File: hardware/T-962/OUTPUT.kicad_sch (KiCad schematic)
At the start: 21 parts

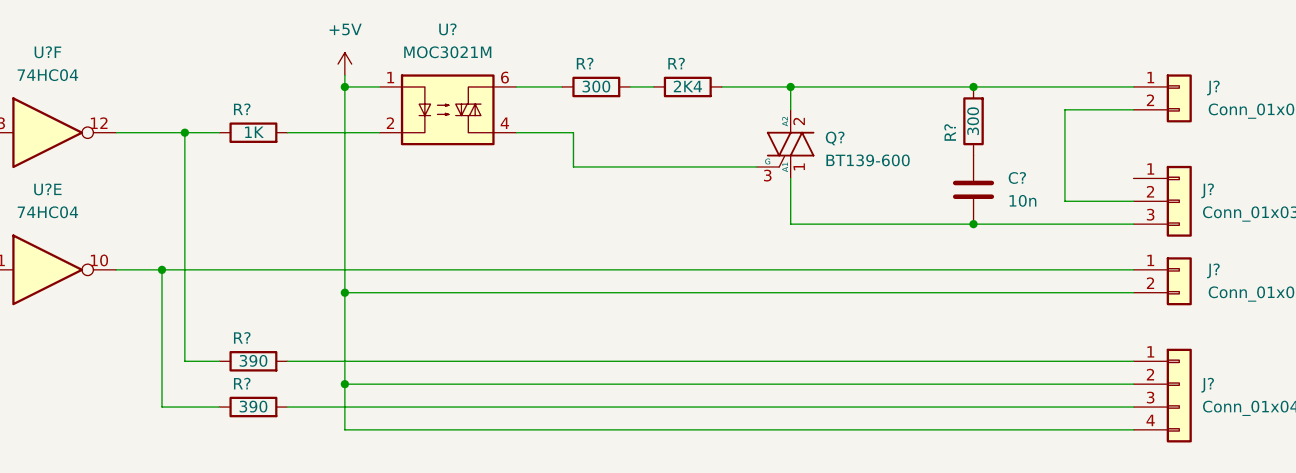
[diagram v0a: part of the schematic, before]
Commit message: add max31850 thermocouple interfaces
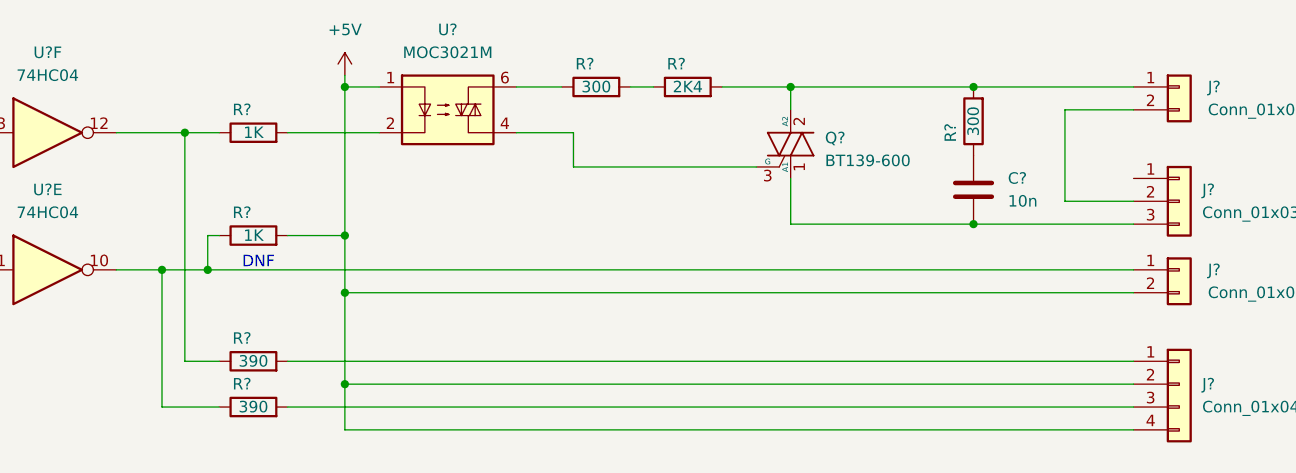
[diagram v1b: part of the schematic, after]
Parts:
- added R?: 1K, symbol Device:R
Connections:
- net +5V: now also R?.2
- net at J?.1 (Pin_1), R?.1, U?.10: now also R?.1
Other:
- note added: "DNF"
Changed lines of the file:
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@@
   (junction (at 144.78 101.6) (diameter 0) (color 0 0 0 0)
   )
+  (junction (at 129.54 99.06) (diameter 0) (color 0 0 0 0)
+  )
   (junction (at 102.87 133.35) (diameter 0) (color 0 0 0 0)
   )
@@
   )
   (junction (at 144.78 111.76) (diameter 0) (color 0 0 0 0)
+  )
+  (junction (at 144.78 95.25) (diameter 0) (color 0 0 0 0)
   )
   (no_connect (at 124.46 148.59))
@@
     (stroke (width 0) (type default) (color 0 0 0 0))
   )
+  (wire (pts (xy 129.54 95.25) (xy 129.54 99.06))
+    (stroke (width 0) (type default) (color 0 0 0 0))
+  )
+  (wire (pts (xy 130.81 95.25) (xy 129.54 95.25))
+    (stroke (width 0) (type default) (color 0 0 0 0))
+  )
+  (wire (pts (xy 129.54 99.06) (xy 232.41 99.06))
+    (stroke (width 0) (type default) (color 0 0 0 0))
+  )
   (wire (pts (xy 148.59 78.74) (xy 144.78 78.74))
     (stroke (width 0) (type default) (color 0 0 0 0))
@@
     (stroke (width 0) (type default) (color 0 0 0 0))
   )
+  (wire (pts (xy 138.43 95.25) (xy 144.78 95.25))
+    (stroke (width 0) (type default) (color 0 0 0 0))
+  )
   (wire (pts (xy 68.58 99.06) (xy 82.55 99.06))
     (stroke (width 0) (type default) (color 0 0 0 0))
@@
     (stroke (width 0) (type default) (color 0 0 0 0))
   )
-  (wire (pts (xy 144.78 78.74) (xy 144.78 101.6))
+  (wire (pts (xy 144.78 78.74) (xy 144.78 95.25))
     (stroke (width 0) (type default) (color 0 0 0 0))
   )
@@
     (stroke (width 0) (type default) (color 0 0 0 0))
   )
+  (wire (pts (xy 144.78 95.25) (xy 144.78 101.6))
+    (stroke (width 0) (type default) (color 0 0 0 0))
+  )
   (wire (pts (xy 194.31 93.98) (xy 194.31 88.9))
     (stroke (width 0) (type default) (color 0 0 0 0))
@@
     (stroke (width 0) (type default) (color 0 0 0 0))
   )
-  (wire (pts (xy 124.46 99.06) (xy 232.41 99.06))
-    (stroke (width 0) (type default) (color 0 0 0 0))
-  )
   (wire (pts (xy 138.43 109.22) (xy 232.41 109.22))
     (stroke (width 0) (type default) (color 0 0 0 0))
@@
     (stroke (width 0) (type default) (color 0 0 0 0))
   )
+  (wire (pts (xy 124.46 99.06) (xy 129.54 99.06))
+    (stroke (width 0) (type default) (color 0 0 0 0))
+  )
   (text "220VAC" (at 254 91.44 0)
     (effects (font (size 1.27 1.27)) (justify left bottom))
@@
   )
   (text "COOLING FAN" (at 254 81.28 0)
+    (effects (font (size 1.27 1.27)) (justify left bottom))
+  )
+  (text "DNF" (at 133.35 99.06 0)
     (effects (font (size 1.27 1.27)) (justify left bottom))
   )
@@
       (effects (font (size 1.27 1.27)) hide)
     )
+    (pin "1")
+    (pin "2")
+  )
+  (symbol (lib_id "Device:R") (at 134.62 95.25 90) (unit 1)
+    (in_bom yes) (on_board yes)
+    (property "Reference" "R?" (id 0) (at 133.35 92.71 90))
+    (property "Value" "1K" (id 1) (at 134.62 95.25 90))
+    (property "Footprint" "" (id 2) (at 134.62 97.028 90)
+      (effects (font (size 1.27 1.27)) hide)
+    )
+    (property "Datasheet" "~" (id 3) (at 134.62 95.25 0)
+      (effects (font (size 1.27 1.27)) hide)
+    )

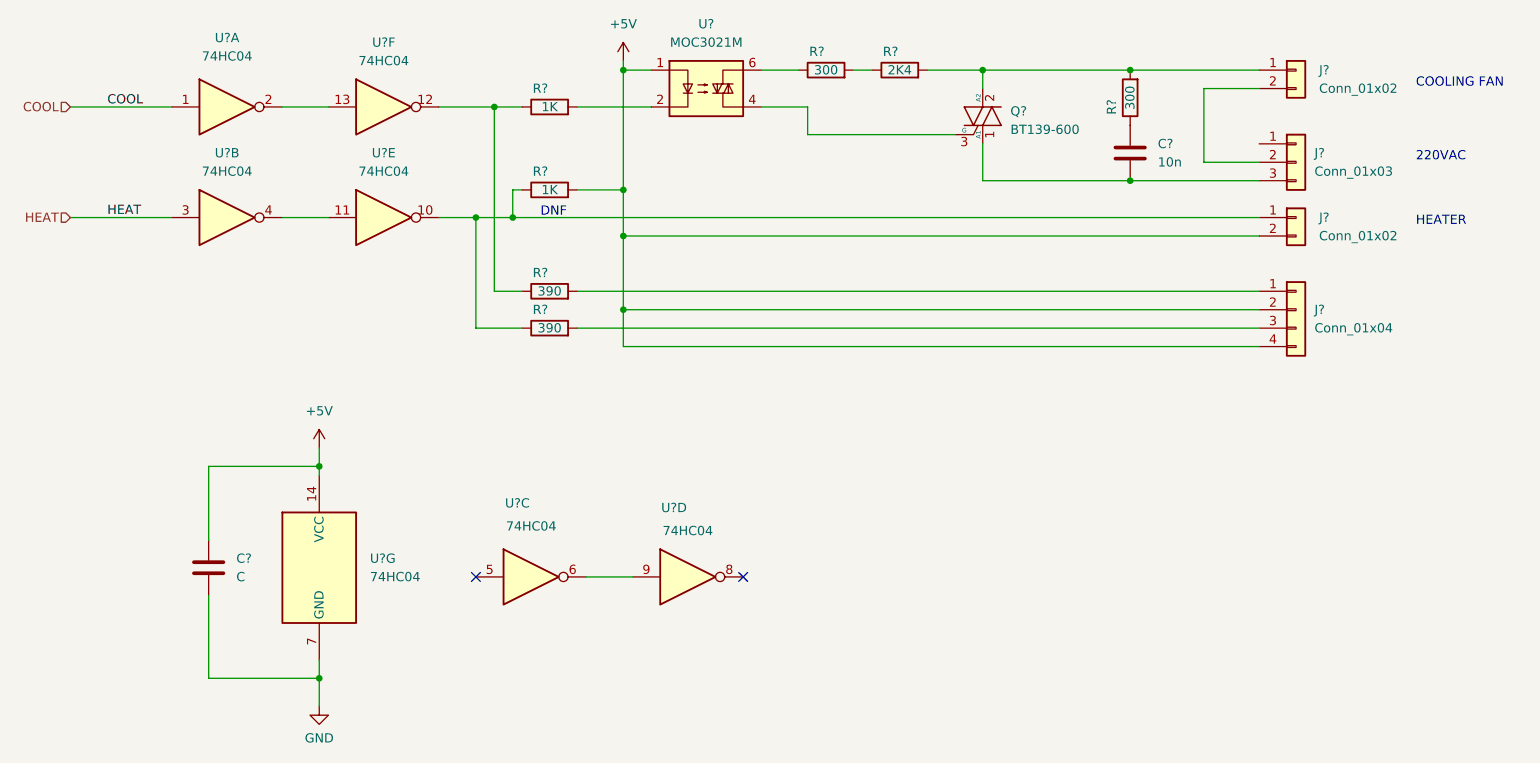
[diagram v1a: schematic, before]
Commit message: fill out designators
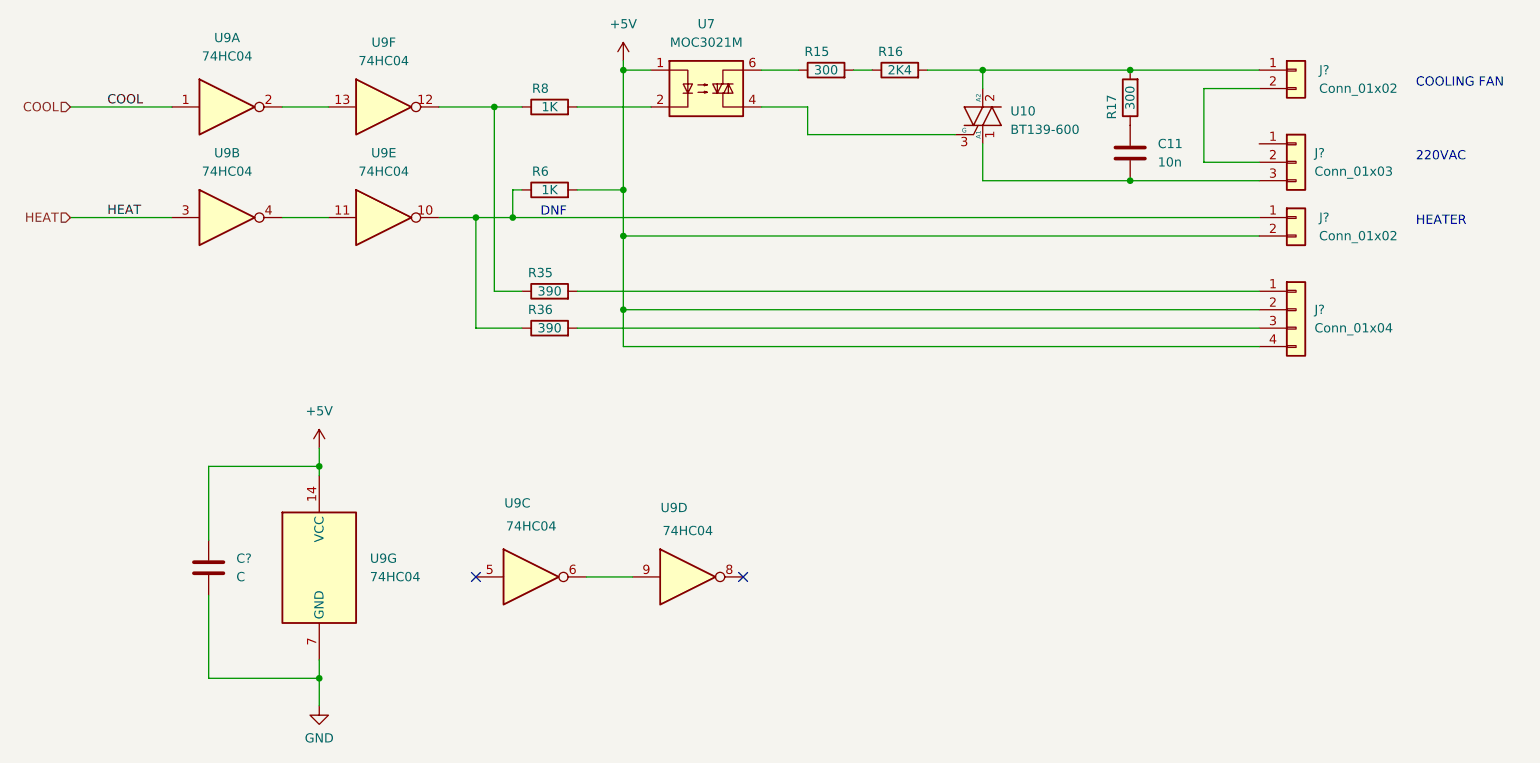
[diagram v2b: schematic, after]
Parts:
- gave numbers to parts that had none: 11
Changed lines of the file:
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@@
   (symbol (lib_id "74xx:74HC04") (at 153.67 148.59 0) (unit 4)
     (in_bom yes) (on_board yes)
-    (property "Reference" "U?" (id 0) (at 151.765 139.065 0))
+    (property "Reference" "U9" (id 0) (at 151.765 139.065 0))
     (property "Value" "74HC04" (id 1) (at 153.67 142.24 0))
     (property "Footprint" "" (id 2) (at 153.67 148.59 0)
@@
   (symbol (lib_id "74xx:74HC04") (at 102.87 147.32 0) (unit 7)
     (in_bom yes) (on_board yes) (fields_autoplaced)
-    (property "Reference" "U?" (id 0) (at 109.855 146.0499 0)
+    (property "Reference" "U9" (id 0) (at 109.855 146.0499 0)
       (effects (font (size 1.27 1.27)) (justify left))
     )
@@
   (symbol (lib_id "74xx:74HC04") (at 90.17 99.06 0) (unit 2)
     (in_bom yes) (on_board yes) (fields_autoplaced)
-    (property "Reference" "U?" (id 0) (at 90.17 90.17 0))
+    (property "Reference" "U9" (id 0) (at 90.17 90.17 0))
     (property "Value" "74HC04" (id 1) (at 90.17 92.71 0))
     (property "Footprint" "" (id 2) (at 90.17 99.06 0)
@@
   (symbol (lib_id "74xx:74HC04") (at 132.08 148.59 0) (unit 3)
     (in_bom yes) (on_board yes)
-    (property "Reference" "U?" (id 0) (at 130.175 138.43 0))
+    (property "Reference" "U9" (id 0) (at 130.175 138.43 0))
     (property "Value" "74HC04" (id 1) (at 132.08 141.605 0))
     (property "Footprint" "" (id 2) (at 132.08 148.59 0)
@@
   (symbol (lib_id "Relay_SolidState:MOC3021M") (at 156.21 81.28 0) (unit 1)
     (in_bom yes) (on_board yes) (fields_autoplaced)
-    (property "Reference" "U?" (id 0) (at 156.21 72.39 0))
+    (property "Reference" "U7" (id 0) (at 156.21 72.39 0))
     (property "Value" "MOC3021M" (id 1) (at 156.21 74.93 0))
     (property "Footprint" "" (id 2) (at 151.13 86.36 0)
@@
   (symbol (lib_id "74xx:74HC04") (at 90.17 83.82 0) (unit 1)
     (in_bom yes) (on_board yes) (fields_autoplaced)
-    (property "Reference" "U?" (id 0) (at 90.17 74.295 0))
+    (property "Reference" "U9" (id 0) (at 90.17 74.295 0))
     (property "Value" "74HC04" (id 1) (at 90.17 76.835 0))
     (property "Footprint" "" (id 2) (at 90.17 83.82 0)
@@
   (symbol (lib_id "Device:R") (at 172.72 78.74 90) (unit 1)
     (in_bom yes) (on_board yes)
-    (property "Reference" "R?" (id 0) (at 171.45 76.2 90))
+    (property "Reference" "R15" (id 0) (at 171.45 76.2 90))
     (property "Value" "300" (id 1) (at 172.72 78.74 90))
     (property "Footprint" "" (id 2) (at 172.72 80.518 90)
@@
   (symbol (lib_id "Device:R") (at 214.63 82.55 180) (unit 1)
     (in_bom yes) (on_board yes)
-    (property "Reference" "R?" (id 0) (at 212.09 83.82 90))
+    (property "Reference" "R17" (id 0) (at 212.09 83.82 90))
     (property "Value" "300" (id 1) (at 214.63 82.55 90))
     (property "Footprint" "" (id 2) (at 216.408 82.55 90)
@@
   (symbol (lib_id "Device:R") (at 182.88 78.74 90) (unit 1)
     (in_bom yes) (on_board yes)
-    (property "Reference" "R?" (id 0) (at 181.61 76.2 90))
+    (property "Reference" "R16" (id 0) (at 181.61 76.2 90))
     (property "Value" "2K4" (id 1) (at 182.88 78.74 90))
     (property "Footprint" "" (id 2) (at 182.88 80.518 90)
@@
   (symbol (lib_id "Device:R") (at 134.62 109.22 90) (unit 1)
     (in_bom yes) (on_board yes)
-    (property "Reference" "R?" (id 0) (at 133.35 106.68 90))
+    (property "Reference" "R35" (id 0) (at 133.35 106.68 90))
     (property "Value" "390" (id 1) (at 134.62 109.22 90))
     (property "Footprint" "" (id 2) (at 134.62 110.998 90)
@@
   (symbol (lib_id "Device:R") (at 134.62 95.25 90) (unit 1)
     (in_bom yes) (on_board yes)
-    (property "Reference" "R?" (id 0) (at 133.35 92.71 90))
+    (property "Reference" "R6" (id 0) (at 133.35 92.71 90))
     (property "Value" "1K" (id 1) (at 134.62 95.25 90))
     (property "Footprint" "" (id 2) (at 134.62 97.028 90)
@@
   (symbol (lib_id "Device:R") (at 134.62 114.3 90) (unit 1)
     (in_bom yes) (on_board yes)
-    (property "Reference" "R?" (id 0) (at 133.35 111.76 90))
+    (property "Reference" "R36" (id 0) (at 133.35 111.76 90))
     (property "Value" "390" (id 1) (at 134.62 114.3 90))
     (property "Footprint" "" (id 2) (at 134.62 116.078 90)
@@
   (symbol (lib_id "74xx:74HC04") (at 111.76 83.82 0) (unit 6)
     (in_bom yes) (on_board yes) (fields_autoplaced)
-    (property "Reference" "U?" (id 0) (at 111.76 74.93 0))
+    (property "Reference" "U9" (id 0) (at 111.76 74.93 0))
     (property "Value" "74HC04" (id 1) (at 111.76 77.47 0))
     (property "Footprint" "" (id 2) (at 111.76 83.82 0)
@@
   (symbol (lib_id "74xx:74HC04") (at 111.76 99.06 0) (unit 5)
     (in_bom yes) (on_board yes) (fields_autoplaced)
-    (property "Reference" "U?" (id 0) (at 111.76 90.17 0))
+    (property "Reference" "U9" (id 0) (at 111.76 90.17 0))
     (property "Value" "74HC04" (id 1) (at 111.76 92.71 0))
     (property "Footprint" "" (id 2) (at 111.76 99.06 0)
@@
   (symbol (lib_id "Triac_Thyristor:BT139-600") (at 194.31 85.09 0) (unit 1)
     (in_bom yes) (on_board yes) (fields_autoplaced)
-    (property "Reference" "Q?" (id 0) (at 198.12 84.4041 0)
+    (property "Reference" "U10" (id 0) (at 198.12 84.4041 0)
       (effects (font (size 1.27 1.27)) (justify left))
     )
@@
   (symbol (lib_id "Device:C") (at 214.63 90.17 0) (unit 1)
     (in_bom yes) (on_board yes) (fields_autoplaced)
-    (property "Reference" "C?" (id 0) (at 218.44 88.8999 0)
+    (property "Reference" "C11" (id 0) (at 218.44 88.8999 0)
       (effects (font (size 1.27 1.27)) (justify left))
     )
@@
   (symbol (lib_id "Device:R") (at 134.62 83.82 90) (unit 1)
     (in_bom yes) (on_board yes)
-    (property "Reference" "R?" (id 0) (at 133.35 81.28 90))
+    (property "Reference" "R8" (id 0) (at 133.35 81.28 90))
     (property "Value" "1K" (id 1) (at 134.62 83.82 90))
     (property "Footprint" "" (id 2) (at 134.62 85.598 90)
